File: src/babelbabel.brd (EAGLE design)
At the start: 41 x 75.5 mm, 152 parts, among them CON1 CON-4P-TABS-JST_GH-RA, CON10 CON-6P-SM06B, CON101 PINHEAD_1X04-2.54, CON102 PINHEAD_1X03-2.54, CON11 PINHEAD_1X04-2.54, CON12 PINHEAD_1X06-2.54, CON15 PINHEAD_1X04-2.54, CON16 CON-4P-TABS-JST_GH-RA, CON2 PINHEAD_1X04-2.54, CON201 PINHEAD_1X04-2.54, CON202 PINHEAD_1X03-2.54, CON3 PINHEAD_1X04-2.54, CON4 USB-AA-PTH, CON5 CON-4P-TABS-JST_GH-RA, CON6 CON-4P-TABS-JST_GH-RA, CON7 USB-1, IC1 NS5B1G385, IC101 STM32F373CBT6-LQFP48, IC102 STM32F373RCT6, IC103 AP2127-3.3, IC105 TJA1051-SO8, IC108 TPD3S014DBVR-SOT23-6, IC13 STM32F103CBT7, IC14 74LVC2T45, IC15 74LVC2T45, IC16 74LVC2T45, IC17 74LVC2T45, IC2 NS5B1G385, IC201 STM32F373CBT6-LQFP48, IC202 STM32F373RCT6, IC203 AP2127-3.3, IC205 TJA1051-SO8, IC208 TPD3S014DBVR-SOT23-6, IC3 AP2127-3.3, IC9 FE1.1S, J1 CONNECTION-SMD, J2 CONNECTION-SMD, Q101 16MHz, Q102 2N7002, Q201 16MHz, Q202 2N7002, Q7 8MHz, Q8 12MHz, Q9 NTZD3152PT1G

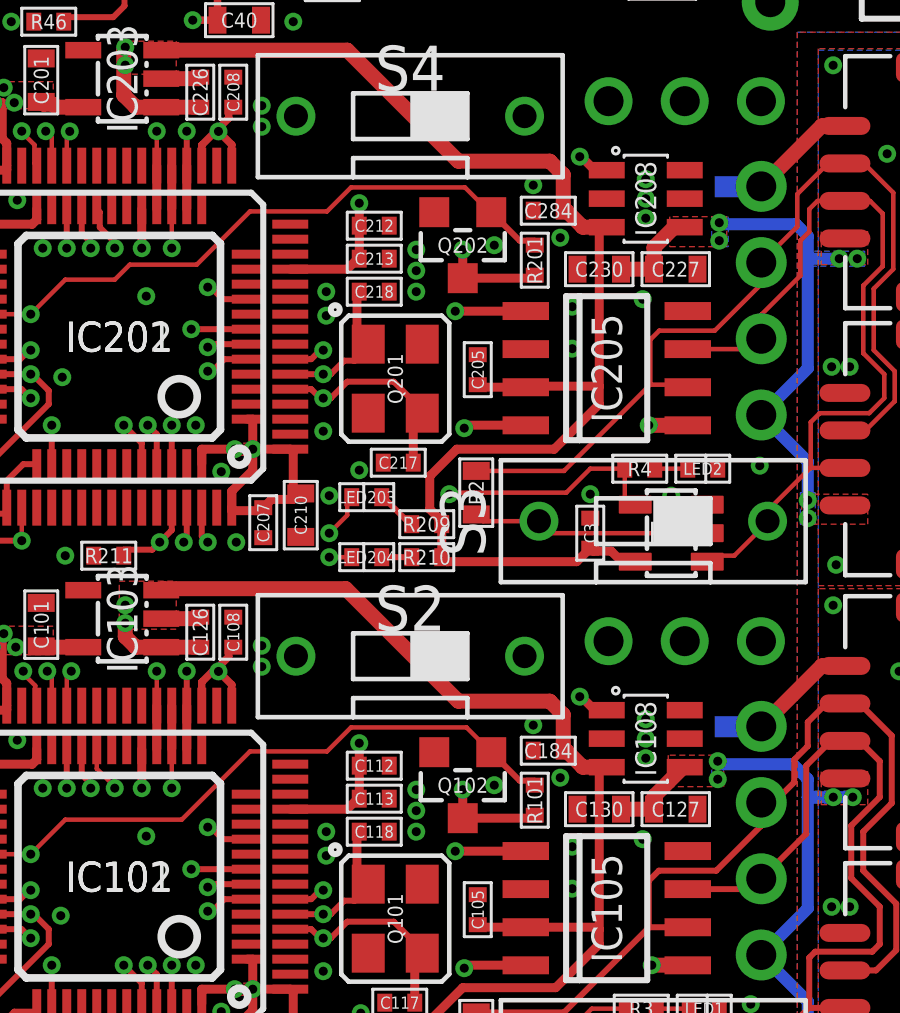
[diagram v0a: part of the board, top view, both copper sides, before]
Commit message: removed mosfet Q2 from both babel, fixes #6
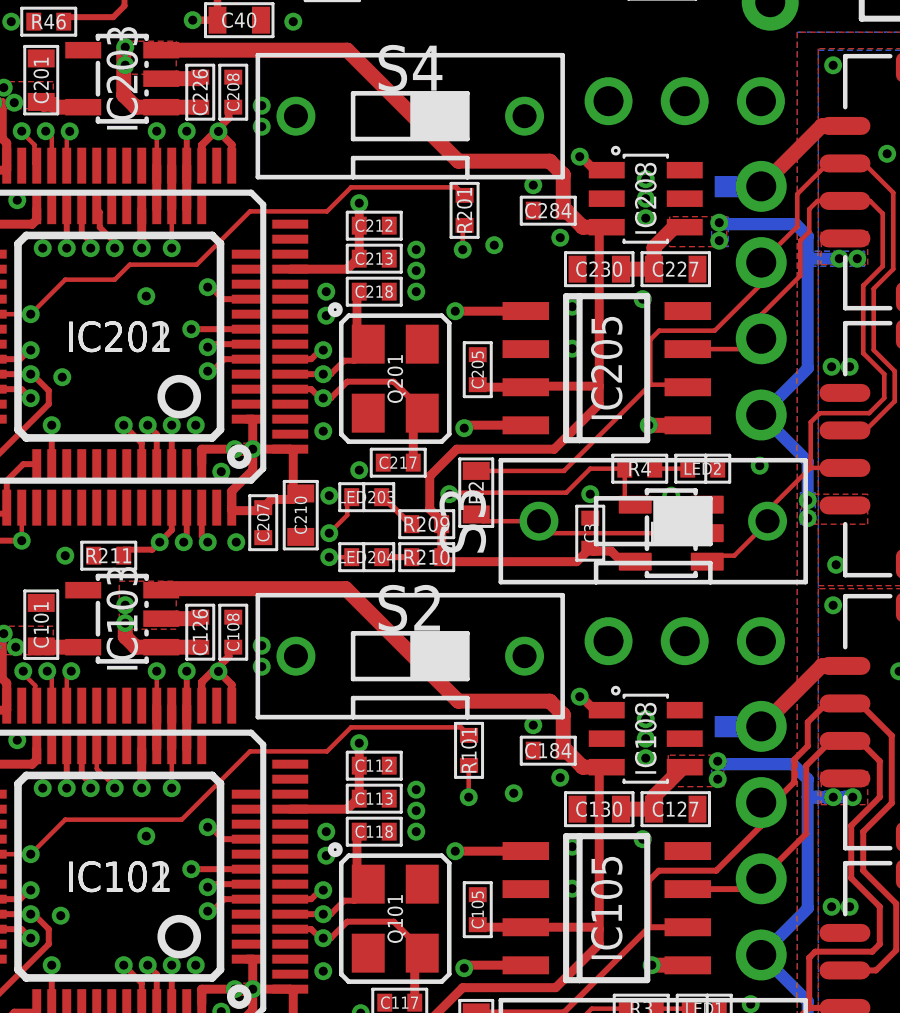
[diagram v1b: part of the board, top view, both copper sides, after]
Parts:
- removed Q102, Q202: 2N7002, mosfet:SOT23
- moved R201 2.87 mm to (23.2, -3.24)
- moved R101 2.75 mm to (23.4, -21.2)
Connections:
- net BABEL1:CAN_VDD_EN: no longer Q102.1
- net BABEL1:VDD_3V3: no longer Q102.3
- net BABEL2:CAN_VDD_EN: no longer Q202.1
- net BABEL2:VDD_3V3: no longer Q202.3
- net GND: no longer Q102.2, Q202.2
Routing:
- net BABEL2:CAN_VDD_EN: track 26.1 -> 23.0 mm
- net BABEL1:CAN_VDD_EN: track 26.1 -> 23.1 mm
- net BABEL2:VDD_3V3: track 92.3 -> 89.7 mm
- net BABEL1:VDD_3V3: track 92.6 -> 90.3 mm

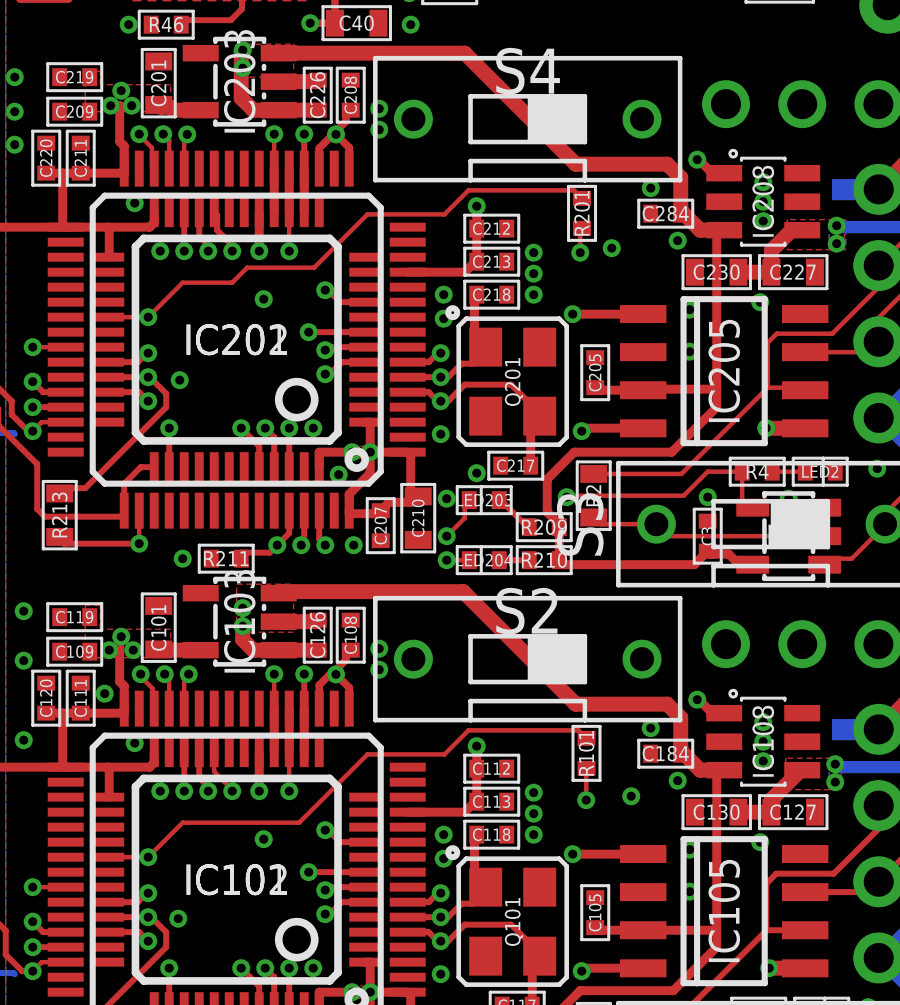
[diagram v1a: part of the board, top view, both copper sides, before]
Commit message: minor routing improvement
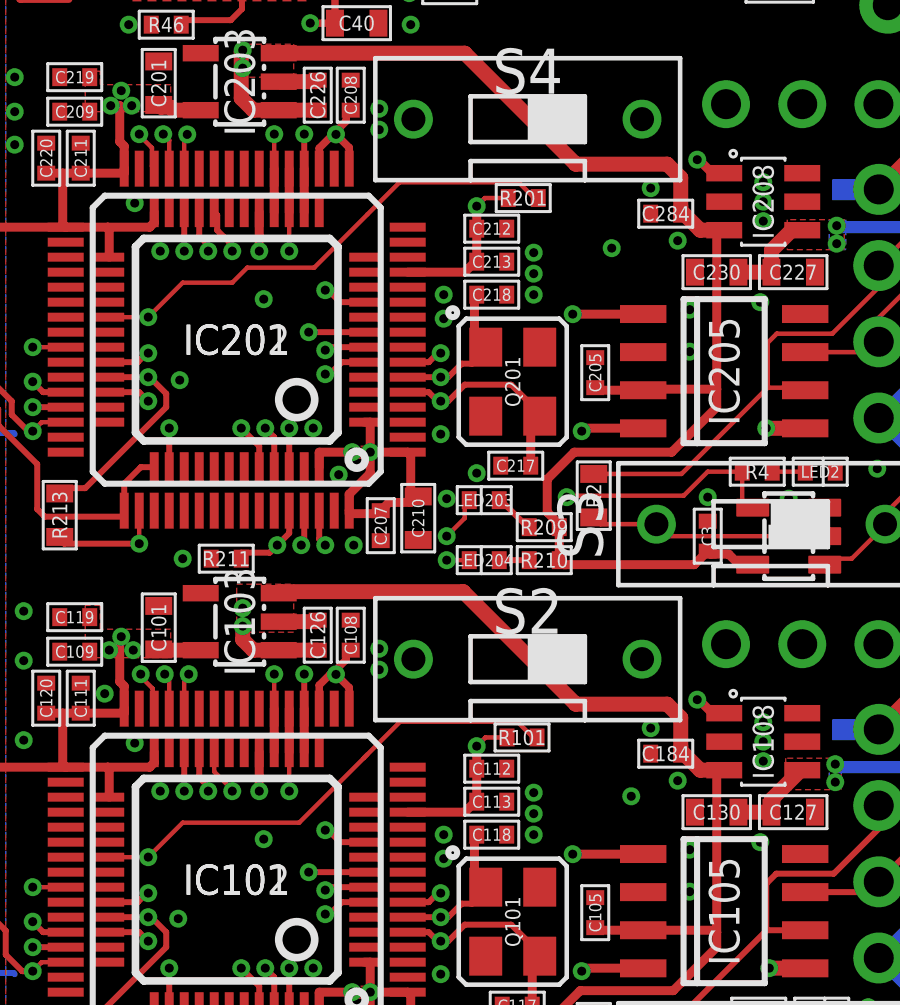
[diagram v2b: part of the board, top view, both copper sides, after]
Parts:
- moved R101 2.21 mm to (21.2, -20.7), turned to 180 degrees
- moved R201 2.03 mm to (21.2, -2.73), turned to 180 degrees
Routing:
- net BABEL1:CAN_VDD_EN: track 23.1 -> 21.9 mm
- net BABEL2:CAN_VDD_EN: track 23.0 -> 21.7 mm
- net BABEL2:VDD_3V3: track 89.7 -> 90.0 mm, vias 12 -> 11
- net BABEL1:VDD_3V3: track 90.3 -> 90.4 mm, vias 12 -> 11

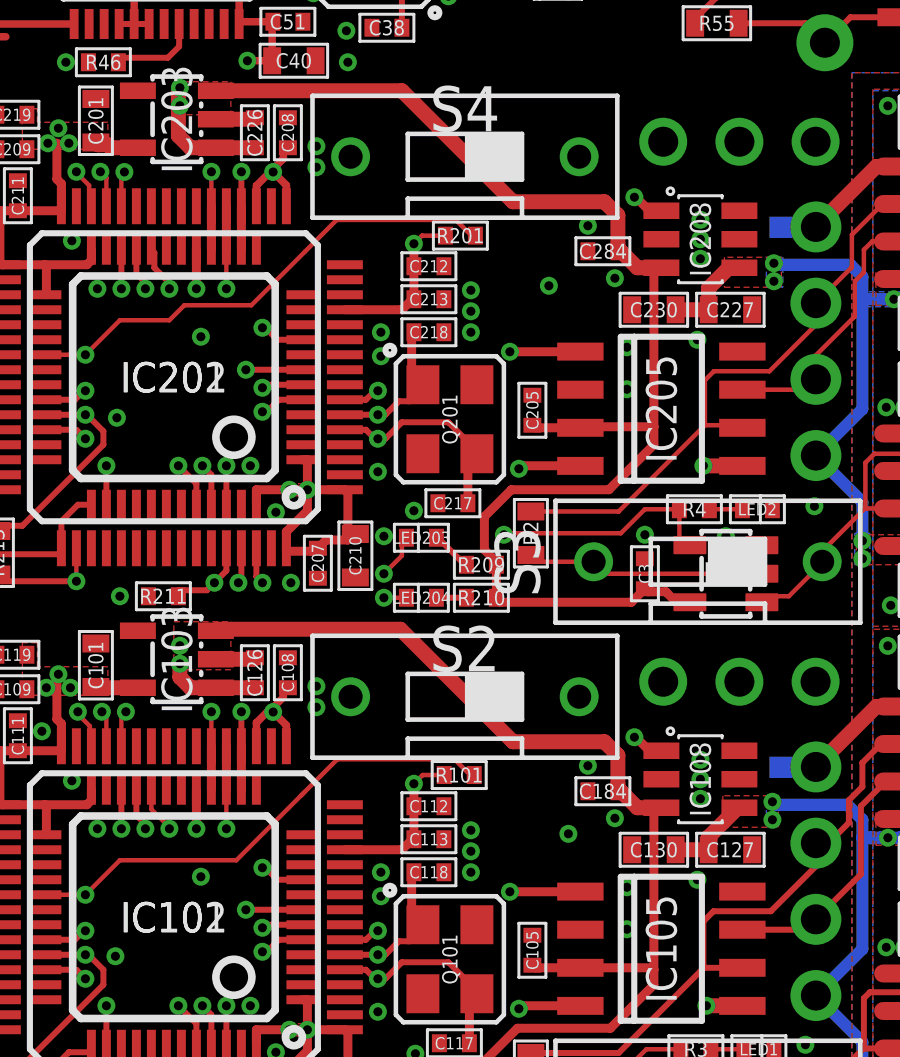
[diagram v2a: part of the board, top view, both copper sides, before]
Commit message: fixes #6
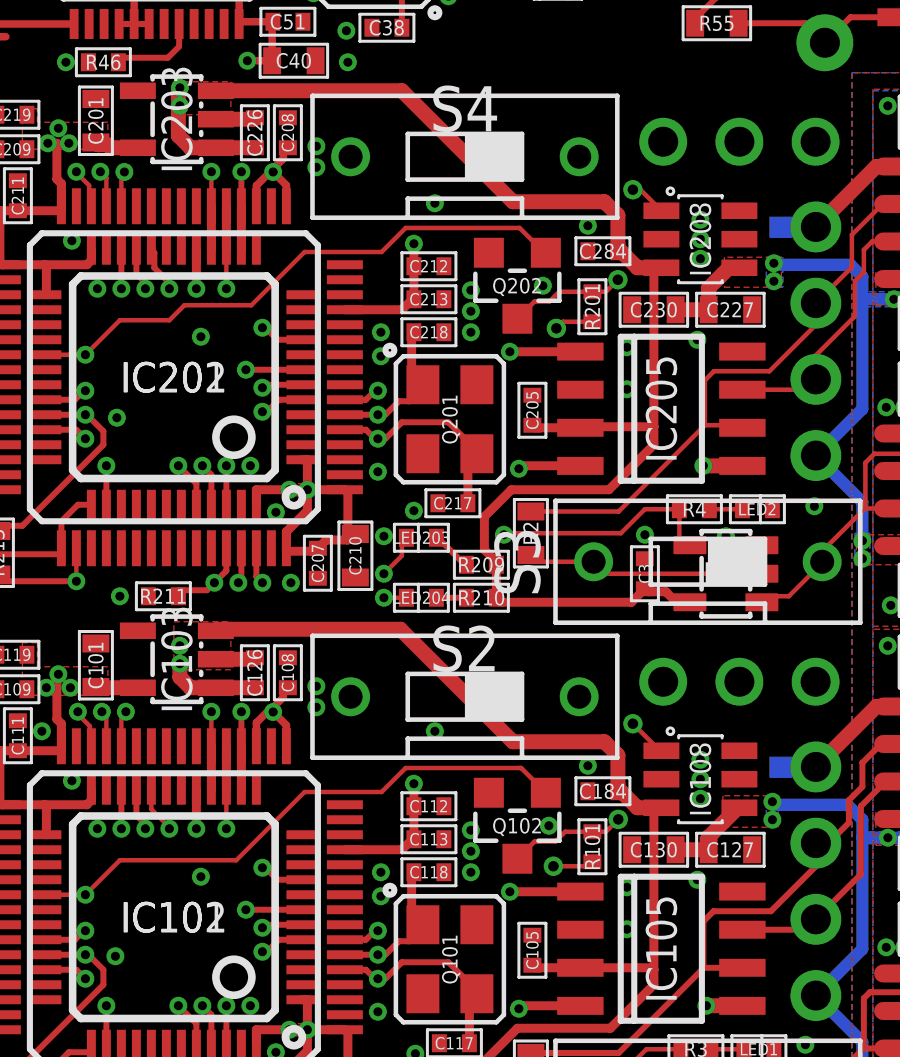
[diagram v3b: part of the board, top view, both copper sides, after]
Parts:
- added Q102, Q202: 2N7002, mosfet:SOT23
- moved R101 5.04 mm to (25.6, -23.1), turned to 270 degrees
- moved R201 5.00 mm to (25.6, -5.10), turned to 270 degrees
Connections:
- new net BABEL1:N$1: IC108.1, Q102.3, R101.1
- new net BABEL2:N$1: IC208.1, Q202.3, R201.1
- net BABEL1:CAN_VDD_EN: now also Q102.1; no longer R101.1
- net BABEL1:VDD_3V3: no longer IC108.1
- net BABEL2:CAN_VDD_EN: now also Q202.1; no longer R201.1
- net BABEL2:VDD_3V3: no longer IC208.1
- net GND: now also Q102.2, Q202.2
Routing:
- net BABEL1:N$1: track 0.00 -> 8.62 mm, vias 0 -> 2
- net BABEL2:N$1: track 0.00 -> 8.34 mm, vias 0 -> 2
- net BABEL2:VDD_3V3: track 90.0 -> 83.0 mm
- net BABEL1:VDD_3V3: track 90.4 -> 83.4 mm
- net BABEL2:CAN_VDD_EN: track 21.7 -> 24.1 mm
- net BABEL1:CAN_VDD_EN: track 21.9 -> 24.1 mm

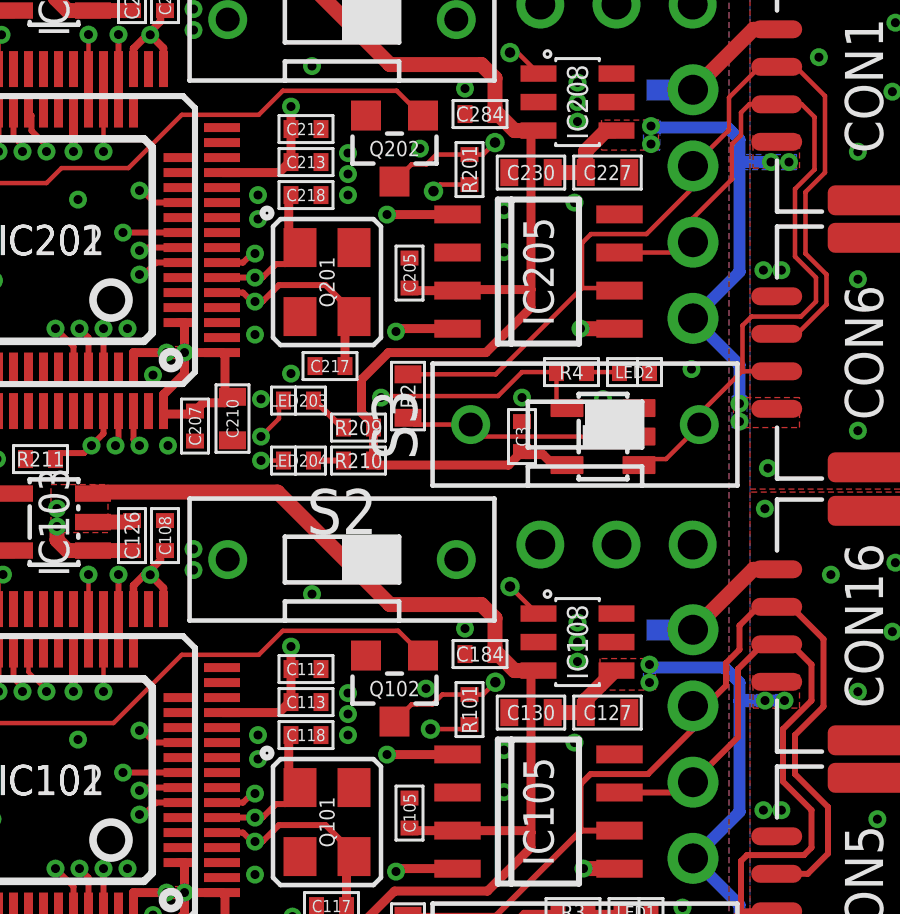
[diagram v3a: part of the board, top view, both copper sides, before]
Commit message: trace width fixes #6
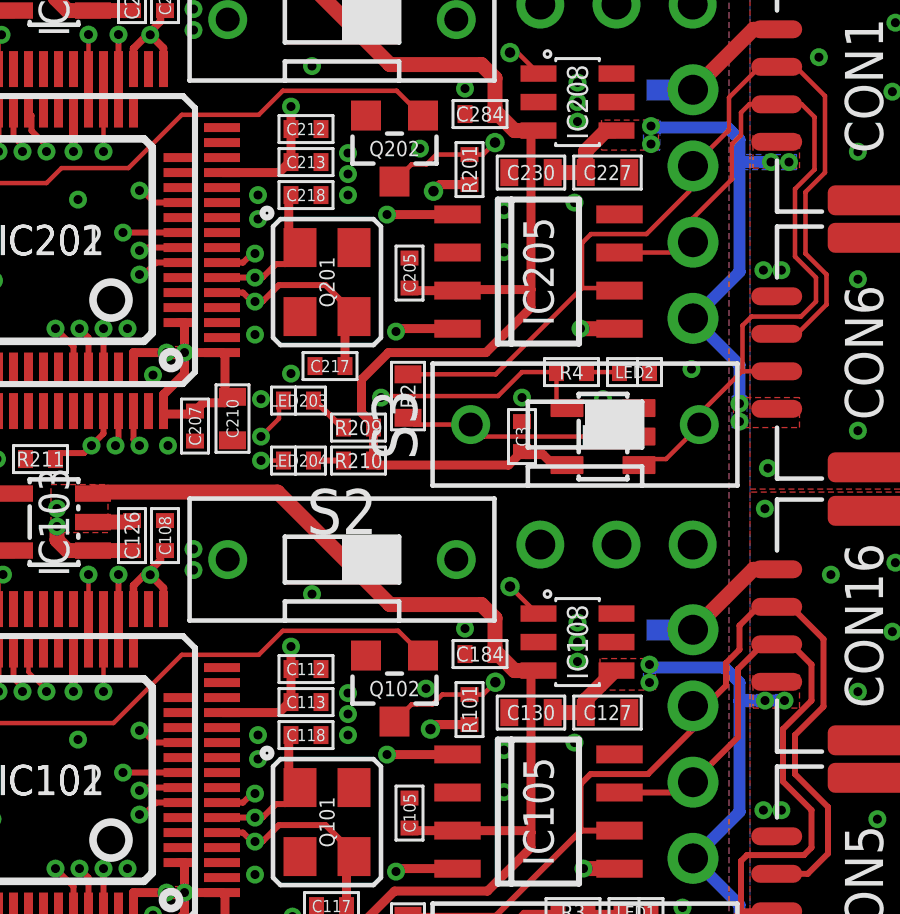
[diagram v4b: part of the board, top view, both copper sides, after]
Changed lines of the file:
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@@
 <contactref element="R101" pad="2"/>
 <via x="24.35" y="-23.75" extent="1-16" drill="0.35"/>
-<wire x1="24.35" y1="-23.75" x2="25.5" y2="-23.75" width="0.1524" layer="1"/>
 <wire x1="25.5" y1="-23.75" x2="25.65" y2="-23.6" width="0.1524" layer="1"/>
+<wire x1="24.35" y1="-23.75" x2="24.5" y2="-23.6" width="0.3048" layer="1"/>
+<wire x1="24.5" y1="-23.6" x2="25.65" y2="-23.6" width="0.3048" layer="1"/>
+<wire x1="7.45" y1="-17.8" x2="6.8" y2="-17.85" width="0" layer="19" extent="1-1"/>
+<wire x1="7.85" y1="-17.35" x2="7.45" y2="-17.8" width="0" layer="19" extent="1-1"/>
+<wire x1="15.55" y1="-29.2" x2="16.15" y2="-29.2" width="0" layer="19" extent="1-1"/>
+<wire x1="8.25" y1="-17.8" x2="7.85" y2="-17.35" width="0" layer="19" extent="1-1"/>
+<wire x1="9.1" y1="-17.775" x2="8.25" y2="-17.8" width="0" layer="19" extent="1-1"/>
+<wire x1="6.8" y1="-16.7" x2="6.8" y2="-17.85" width="0" layer="19" extent="1-1"/>
 </signal>
 <signal name="BABEL1:PA4">
@@
 <wire x1="24.45" y1="-5.85" x2="24.45" y2="-5.82" width="0.1524" layer="15"/>
 <via x="24.45" y="-5.82" extent="1-16" drill="0.35"/>
-<wire x1="24.45" y1="-5.82" x2="24.67" y2="-5.6" width="0.1524" layer="1"/>
-<wire x1="24.67" y1="-5.6" x2="25.65" y2="-5.6" width="0.1524" layer="1"/>
+<wire x1="24.45" y1="-5.82" x2="24.67" y2="-5.6" width="0.3048" layer="1"/>
+<wire x1="24.67" y1="-5.6" x2="25.65" y2="-5.6" width="0.3048" layer="1"/>
+<wire x1="8.2" y1="0.35" x2="7.85" y2="0.85" width="0" layer="19" extent="1-1"/>
+<wire x1="15.55" y1="-11.2" x2="16.15" y2="-11.2" width="0" layer="19" extent="1-1"/>
+<wire x1="7.5" y1="0.35" x2="7.85" y2="0.85" width="0" layer="19" extent="1-1"/>
+<wire x1="6.8" y1="0.15" x2="7.5" y2="0.35" width="0" layer="19" extent="1-1"/>
+<wire x1="9.1" y1="0.375" x2="8.2" y2="0.35" width="0" layer="19" extent="1-1"/>
+<wire x1="6.8" y1="1.3" x2="7.85" y2="0.85" width="0" layer="19" extent="1-1"/>
 </signal>
 <signal name="BABEL2:PA4">
